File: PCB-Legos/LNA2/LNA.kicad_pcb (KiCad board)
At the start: 4 copper layers, 50.8 x 27.9 mm, 35 parts, among them J1 Conn_Coaxial, J2 Conn_Coaxial, J3 Conn_Coaxial, U1 LP2, U2 LNA, U3 QPQ, U4 LP2, U5 LNA, U6 QPQ

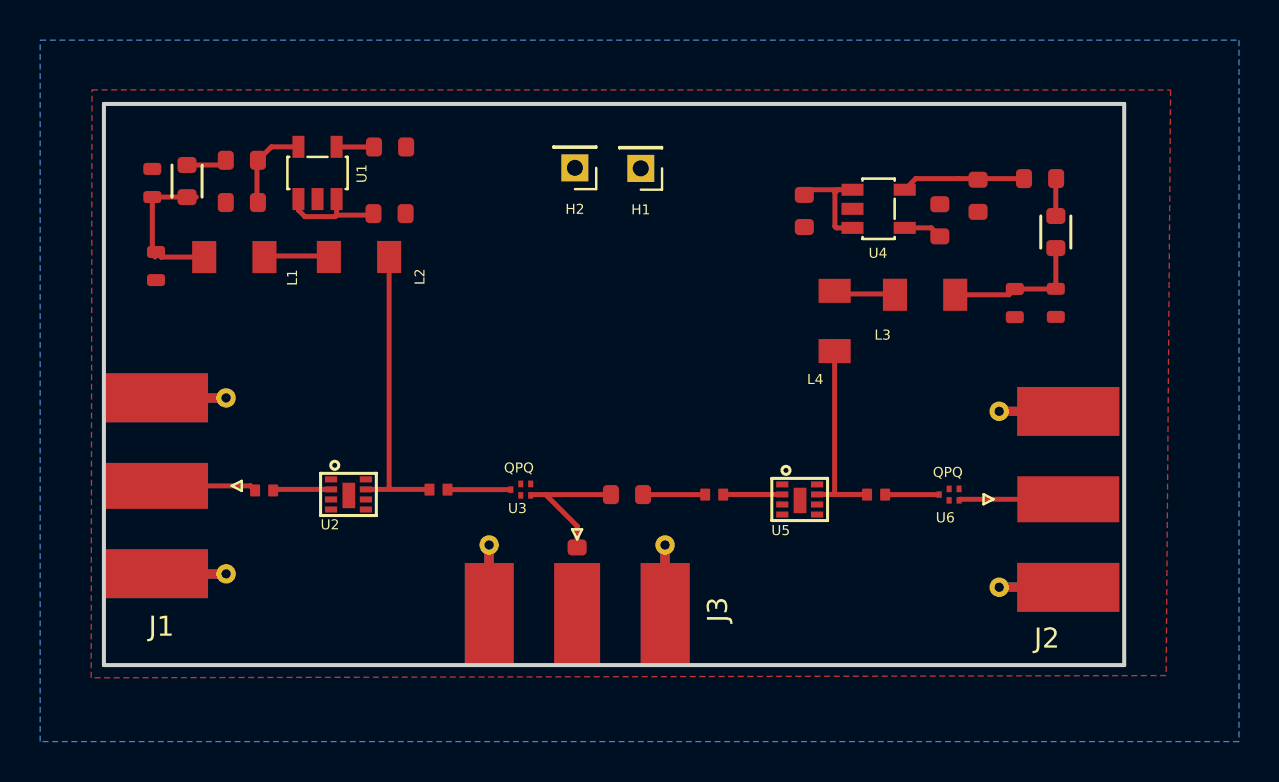
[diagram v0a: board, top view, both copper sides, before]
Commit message: LNA
Fixed minor issues in RF path.
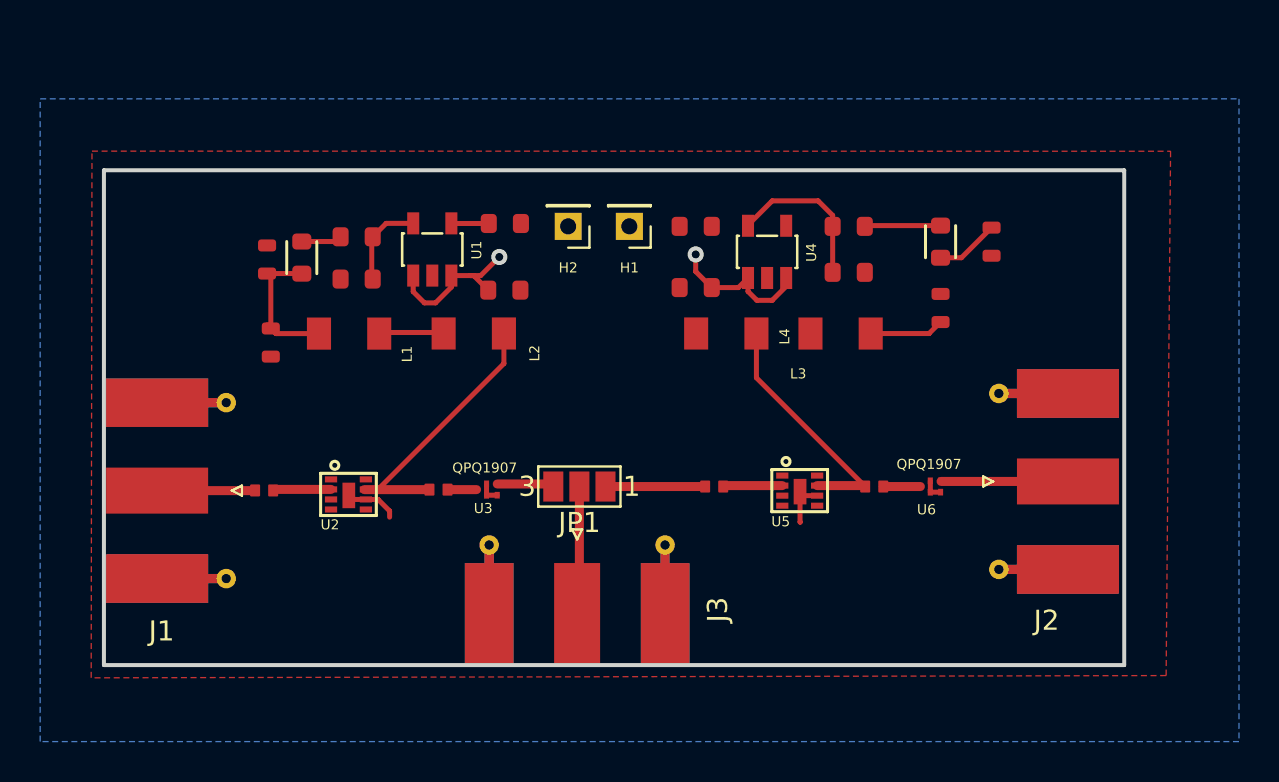
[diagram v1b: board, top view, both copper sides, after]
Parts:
- removed R3, R4: 0Ω, HGS_Reflector:.0603-B-NOSILK
- added JP1: SolderJumper_3_Open, Jumper:SolderJumper-3_P1.3mm_Open_Pad1.0x1.5mm_NumberLabels, F.Cu at (135.4, 82.5)
- C11: value 10nF -> 10 nF
- C12: value 2.2uF -> 2.2 uF
- C13, C14, C2, C6, C7, C9: value .1nF -> 100 pF
- C3, C8: value 1uF -> 1 uF
- E1, E2: value BLM -> BLM18GG471SZ1D
- H2: value VDD -> VUSB
- R1: value 0Ω -> 0
- U1, U4: value LP2 -> LP2985XX-N
- U2, U5: value LNA -> LNA-TP3M9037
- U3, U6: value QPQ -> QPQ1907
- moved C11 12.2 mm to (141.2, 69.6), turned to 180 degrees
- moved R2 9.82 mm to (148.8, 69.6)
- moved C12 7.48 mm to (148.8, 71.9), turned to 0 degrees
- moved L2 6.87 mm to (130.2, 74.9)
- moved C5 6.87 mm to (124.3, 72.2)
- moved C8 6.87 mm to (120.1, 75.4)
- moved E1 6.87 mm to (121.6, 71.2)
- moved L1 6.87 mm to (124.0, 74.9)
- moved R1 6.87 mm to (124.3, 70.1)
- moved C4 6.87 mm to (131.7, 69.5)
- moved C7 6.87 mm to (119.9, 71.2)
- moved C10 6.87 mm to (131.7, 72.8)
- moved U1 6.87 mm to (128.1, 70.7)
- moved C3 6.62 mm to (141.2, 72.6), turned to 0 degrees
- moved U4 5.95 mm to (144.8, 70.9), turned to 90 degrees
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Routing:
- net GND: track 0.00 -> 7.31 mm
- net Net-(J3-Pad1): track 0.00 -> 6.40 mm
- net VUSB: track 10.6 -> 15.3 mm, vias 0 -> 2
- net Net-(U3-PadOUTPUT): track 7.29 -> 2.84 mm
- net Net-(L3-Pad1): track 2.86 -> 0.00 mm
- net Net-(C13-Pad1): track 9.65 -> 12.3 mm
- net Net-(C2-Pad1): track 7.21 -> 4.88 mm
- net Net-(C11-Pad1): track 1.92 -> 0.00 mm
- net Net-(E2-Pad1): track 1.87 -> 3.79 mm
- net Net-(C9-Pad1): track 3.09 -> 4.96 mm
- net Net-(C12-Pad1): track 6.17 -> 7.88 mm
- net Net-(C6-Pad2): track 3.15 -> 1.45 mm
- net Net-(J2-Pad1): track 5.46 -> 6.35 mm
- net Net-(C13-Pad2): track 2.69 -> 1.85 mm
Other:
- board size 50.8 x 27.9 mm -> 50.8 x 24.6 mm
